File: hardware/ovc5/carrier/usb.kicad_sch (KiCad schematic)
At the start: 100 parts, among them J1 USB_C_Receptacle, U10 S25FL064, U2 CYUSB43x7, U5 USB3_A_Dual_Stacked, U8 TPS2561, Y1 25MHz

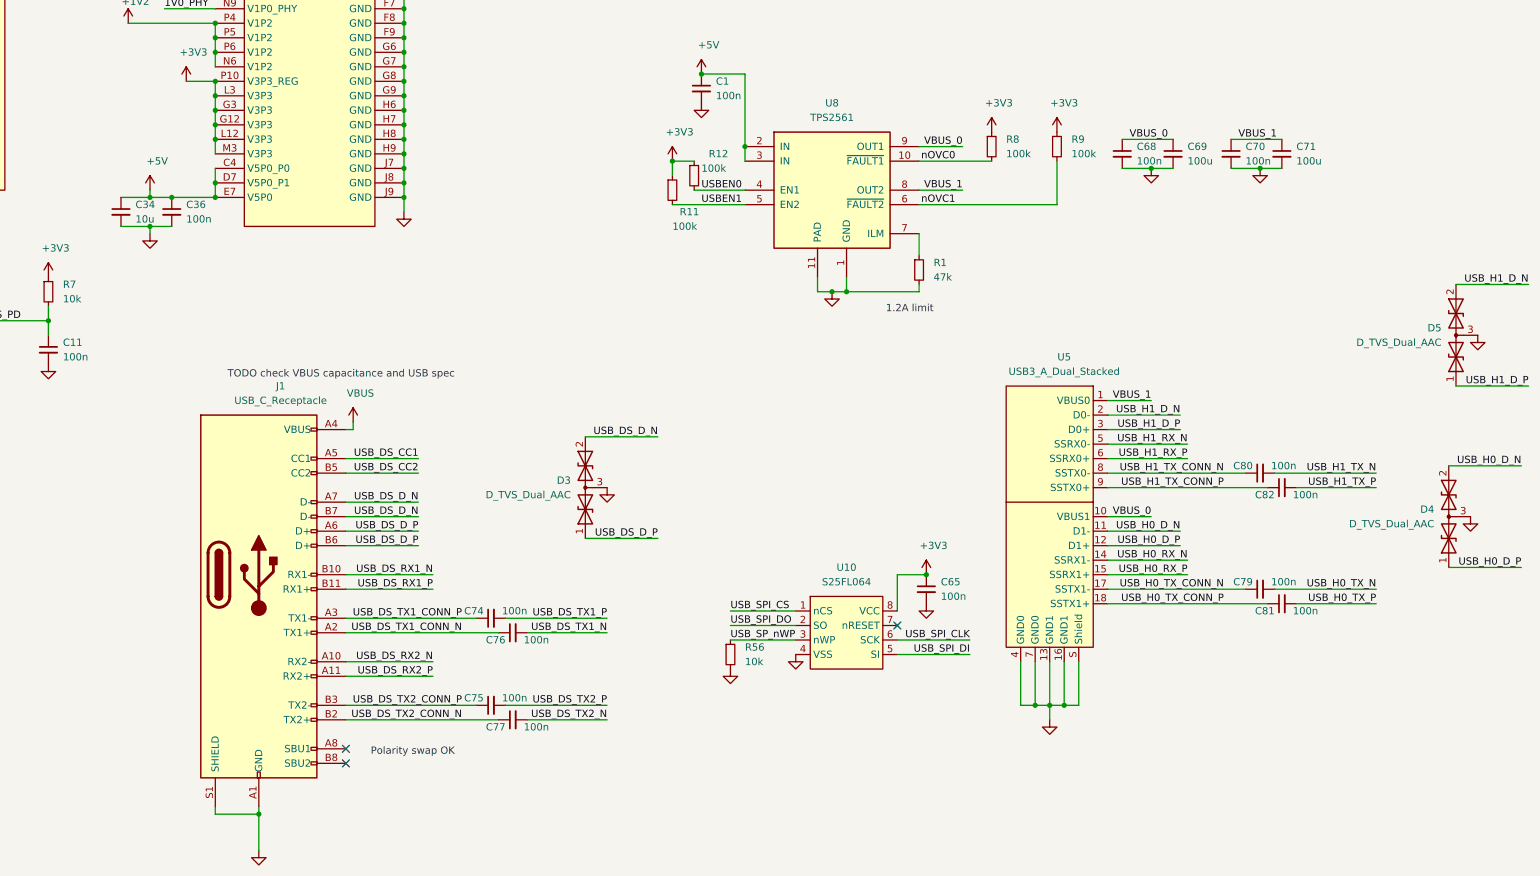
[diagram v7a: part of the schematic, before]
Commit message: Address review feedback
* Increase capacitance on VBUS host lines
* Add ferrite beads to VBUS host lines
* Add capacitance to VBUS device line
* Add shield RC filtering circuit on USB connectors
* Add stitching vias to perimeter of PCB
* Switch CAM0 and CAM3 FPGA lines for simpler routing
* Add ground vias next to USB3 data lines vias

Signed-off-by: Luca Della Vedova <luca@openrobotics.org>
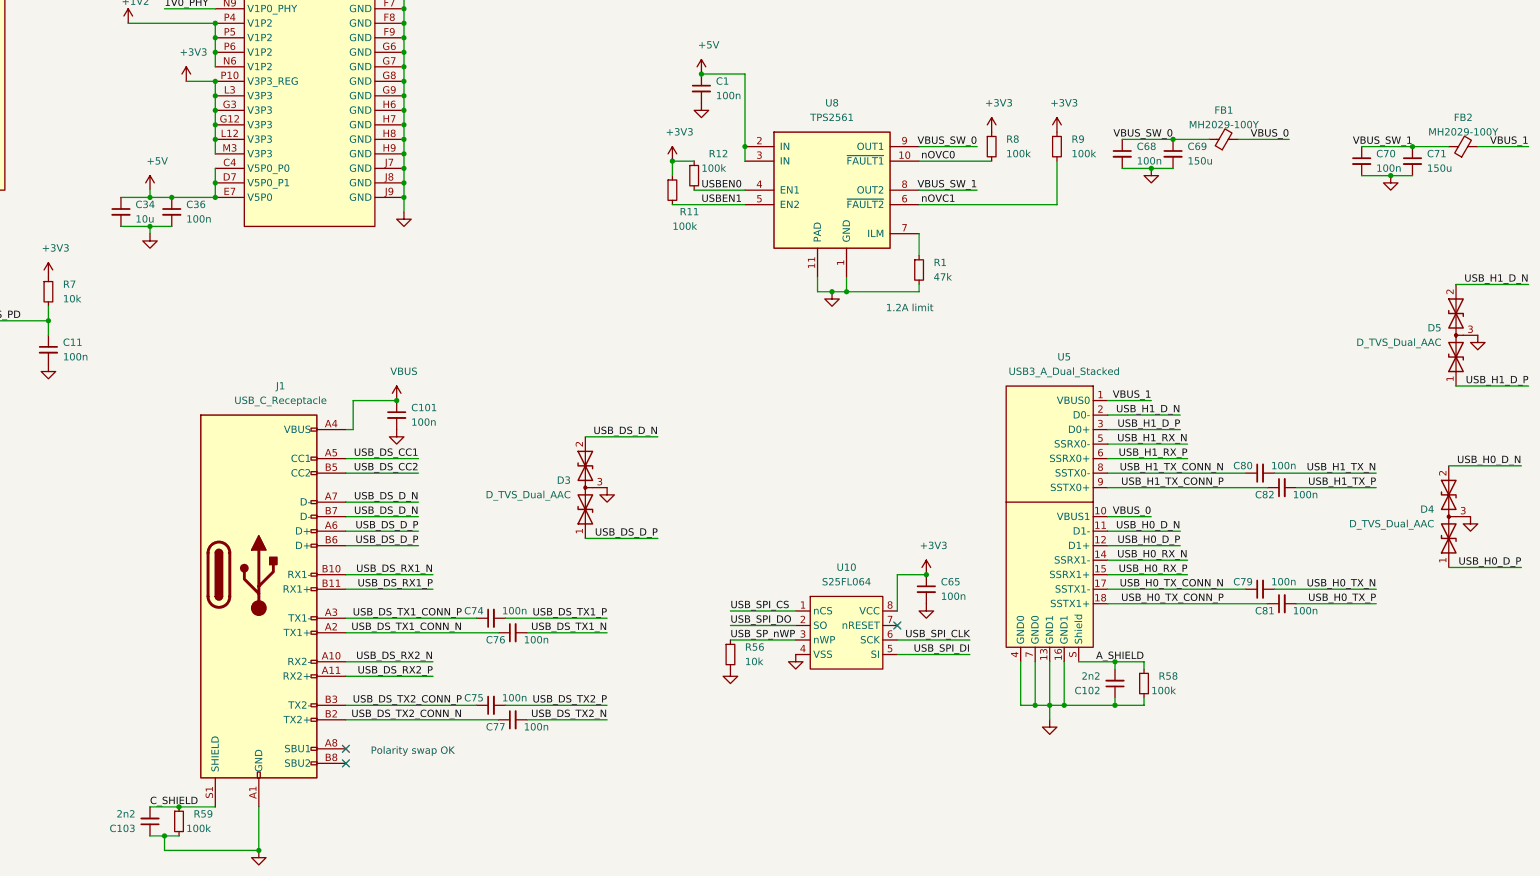
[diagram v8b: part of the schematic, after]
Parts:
- added C101: 100n, Capacitor_SMD:C_0402_1005Metric, symbol Device:C_Small
- added C102, C103: 2n2, Capacitor_SMD:C_0402_1005Metric, symbol Device:C_Small
- added FB1, FB2: MH2029-100Y, Inductor_SMD:L_0805_2012Metric, symbol Device:FerriteBead_Small
- added R58, R59: 100k, Resistor_SMD:R_0402_1005Metric, symbol Device:R_Small
- C69, C71: value 100u -> 150u; footprint Capacitor_SMD:C_1206_3216Metric -> Capacitor_SMD:C_Elec_6.3x7.7; D1PN 445-6007-1-ND -> PCE4401CT-ND; MPN C3216X5R1A107M160AC -> EEE-FKC151XAP
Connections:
- net GND: now also C101.2, C102.1, C103.1, R58.2, R59.2; no longer J1.S1 (SHIELD), U5.S (Shield)
- net VBUS: now also C101.1
- net VBUS_0: now also FB1.2; no longer C68.1, C69.1, U8.9 (OUT1)
- net VBUS_1: now also FB2.2; no longer C70.1, C71.1, U8.8 (OUT2)
- new net A_SHIELD: C102.2, R58.1, U5.S (Shield)
- new net C_SHIELD: C103.2, J1.S1 (SHIELD), R59.1
- new net VBUS_SW_0: C68.1, C69.1, FB1.1, U8.9 (OUT1)
- new net VBUS_SW_1: C70.1, C71.1, FB2.1, U8.8 (OUT2)
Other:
- note removed: "TODO check VBUS capacitance and USB spec"
- moved on the sheet: C70, C71
